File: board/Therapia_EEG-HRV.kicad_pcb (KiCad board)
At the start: 4 copper layers, 61.8 x 45 mm, 135 parts

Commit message: S4a: synthesize the 6 NPTH holes and close the board outline
13_fix_import.py repairs three EasyEDA-importer artefacts:
- the four M2 mounting holes were PTH pads; they become NPTH H1..H4,
  excluded from BOM/POS
- the two USB-C pegs were Edge.Cuts polygons owned by J1; they become
  standalone NPTH footprints PEG1/PEG2 at the same centres
- the board outline arrived as three open segments (EasyEDA holds it as one
  closed POLY); the rectangle is redrawn at the exact 2434x1772 mil size

Gate gates/S4a.json 10/10: NPTH 6 holes matching the 2026-08-16 DRL within
2um, PTH 16 and vias 238 unchanged, Edge.Cuts exactly 4 segments.
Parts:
- added PEG1: NPTH_0.7000mm_peg, NPTH_0.7mm_USB-C_peg, F.Cu at (176.9, 113.9)
- added PEG2: NPTH_0.7000mm_peg, NPTH_0.7mm_USB-C_peg, F.Cu at (176.9, 108.1)
- H1, H2, H3, H4: renamed from ?; value (none) -> NPTH_2.3876mm_M2

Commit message: S3: freeze ACCEPTANCE.md, generate the JLC rules, prove they see L1-L4
- ACCEPTANCE.md defines 'ready to order' as gates A..G; it is the spec the
  final check will implement. Records one deliberate deviation from the brief:
  pad_to_mask_clearance 0.0508 not 0.1016, because 4 mil per side leaves a
  0.0168 mm mask dam on the ADS1299's 0.5 mm pitch.
- 14_make_rules.py generates .kicad_pro + .kicad_dru + the board (setup) block
  from one table. Cross-checks contract/easyeda_rules.json and shows EasyEDA
  labels those values mm while storing mil (defInner 6.0039 -> 0.305 mm drill).
- 15_gate_s3.py runs DRC and requires L1..L4 to come back out of it. All four
  are reported, each at 0.0000 mm actual clearance.
- lib/drc.py: kicad-cli DRC is not deterministic (523/525/526 on identical
  input), so gates compare (type, nets, refs) signatures, not counts.

DRC baseline with JLC rules: 526 violations, 68 error, 0 unconnected
(was 1025/545 against KiCad defaults).
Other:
- rule pad_to_mask_clearance: 0 -> 0.0508
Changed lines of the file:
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@@
 	)
 	(setup
-		(pad_to_mask_clearance 0)
+		(pad_to_paste_clearance 0)
+		(solder_mask_min_width 0.0508)
+		(pad_to_mask_clearance 0.0508)
 		(allow_soldermask_bridges_in_footprints no)
 		(tenting

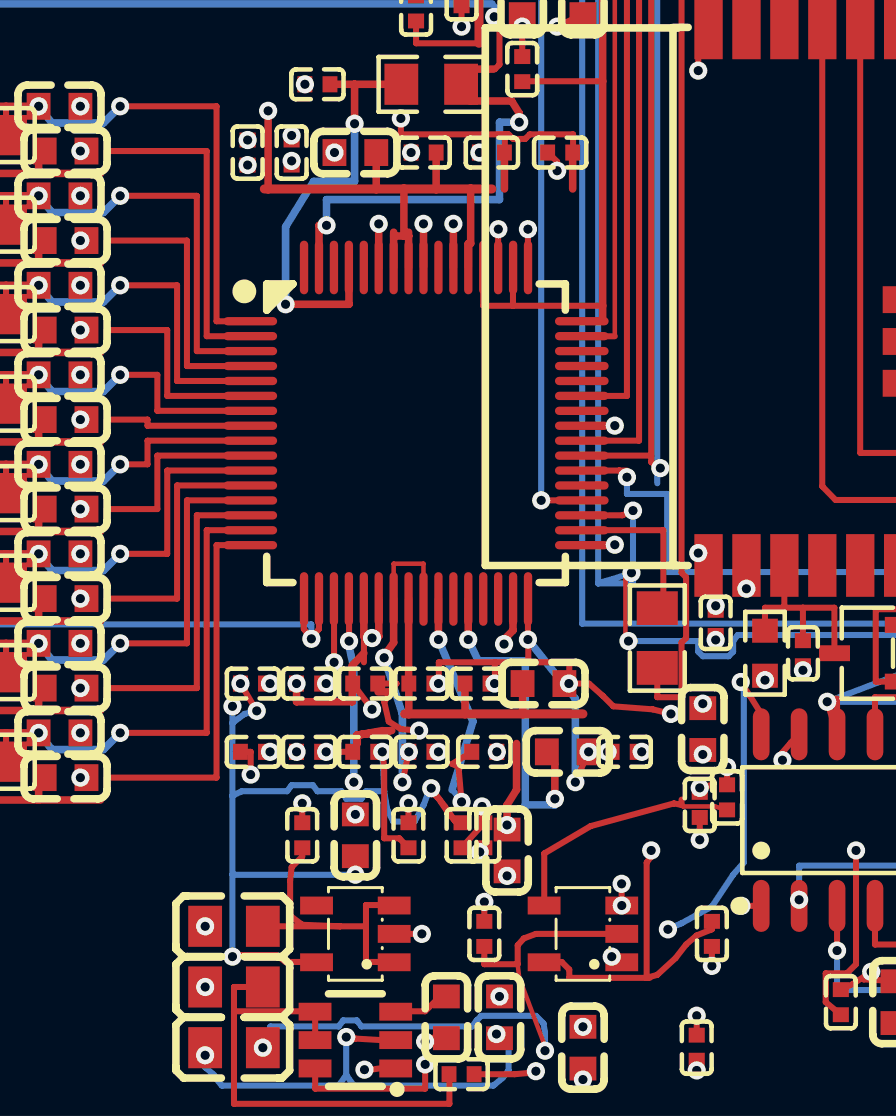
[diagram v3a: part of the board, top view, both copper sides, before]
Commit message: S4: apply ECO-1/2/3 to the PCB
ECO-1 (8 pins): TPS72325 EN moves off GND onto V_NLDO_IN -- the fatal B1 that
kept AVSS from ever coming up -- plus RESV1 to GND, GPIO1-4 bundled to the
adjacent GND pin, and VCAP2/VCAP3 onto new nets.
ECO-1 (4 parts): C_VCAP2/C_VCAP3/C_VCAP3_H/C_VCAP1_H placed and routed.
ECO-3 (2 parts): C_VCAP1 and C_VREFP_10u to 1206. Both only fit rotated 90.
ECO-2: values and LCSC numbers, no copper change. All 135 parts now carry
Value/MPN/LCSC from data/parts_lcsc.csv.

Result: pad net map == contract (0 diffs), 0 unconnected, DRC errors equal to
the pre-ECO baseline. Parts 137->141, tracks 1191->1213, vias 238->240.

lib/route.py does the geometry: every track, via and footprint position is
checked against the real copper at the design-rule clearance before it is
placed, and a step that cannot be satisfied is reported rather than forced.
lib/drc.py compares DRC reports by (type, nets) signature because kicad-cli
returns 525-531 violations for the same board on consecutive runs.
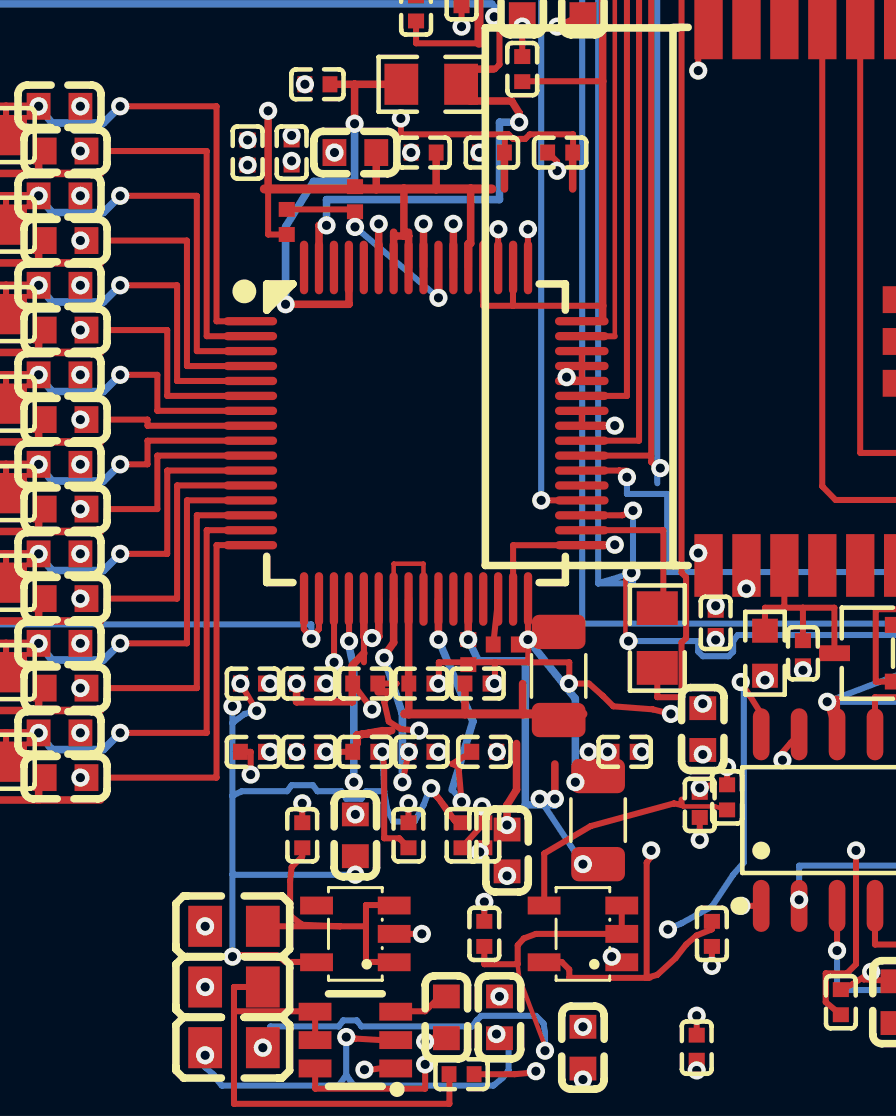
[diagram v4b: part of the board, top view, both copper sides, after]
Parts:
- removed the C_VREFP_10u at (150.4, 110.5)
- added C_VCAP1_H: 100nF, ProPrj_The-easyedapro:C0402, F.Cu at (147.9, 109.4)
- added C_VCAP2: 1uF, ProPrj_The-easyedapro:C0402, F.Cu at (149.2, 109.2)
- added C_VCAP3: 1uF, ProPrj_The-easyedapro:C0402, F.Cu at (144.1, 94.3)
- added C_VCAP3_H: 100nF, ProPrj_The-easyedapro:C0402, F.Cu at (141.8, 95.0)
- added C_VREFP_10u: 10uF_25V, C_1206_3216Metric, F.Cu at (150.9, 110.2)
- AMS1117: value (none) -> AMS1117-3.3
- C_3V3_B, C_3V3_B2, C_3V3_OUT, C_AVDD1_10u, C_AVDD_B, C_AVSS_B, C_BULK, C_DVDD_10u, C_DVDD_B, C_LM_FLY, C_LM_OUT, C_USB5V_B: value (none) -> 10uF
- C_3V3_H, C_3V3_H2, C_AVDD1_100n, C_AVDD_H, C_AVDD_P19, C_AVDD_P3, C_AVDD_P31, C_AVDD_P36, C_AVDD_P59, C_AVDD_P64, C_AVSS_H, C_AVSS_P17, C_AVSS_P30, C_AVSS_P37, C_AVSS_P60, C_BIAS_INV, C_DVDD_H, C_DVDD_P40, C_DVDD_P58, C_EN_DLY, C_HF, C_RST_DLY, C_USB5V_H, C_USB_V3, C_USB_VCC, C_VREFP_100n: value (none) -> 100nF
- C_3V3_IN, C_3V3_M, C_AVDD1_1u, C_LM_IN, C_NLDO_IN, C_PLDO_IN, C_PLDO_OUT, C_VCAP4: value (none) -> 1uF
- C_AVDD1_10n, C_VREFP_10n: value (none) -> 100pF
- C_CM1N, C_CM1P, C_CM2N, C_CM2P, C_CM3N, C_CM3P, C_CM4N, C_CM4P, C_CM5N, C_CM5P, C_CM6N, C_CM6P, C_CM7N, C_CM7P, C_CM8N, C_CM8P: value (none) -> 1nF
- C_DIF1, C_DIF2, C_DIF3, C_DIF4, C_DIF5, C_DIF6, C_DIF7, C_DIF8: value (none) -> 10nF_NP0_50V
- C_NLDO_OUT: value (none) -> 2.2uF
- C_NR: value (none) -> 10nF
- C_VCAP1: value (none) -> 100uF; footprint ProPrj_The-easyedapro:C0603 -> C_1206_3216Metric
- D_ESD: value (none) -> USBLC6-2SC6
- D_LED: value (none) -> LED_Y
- F1: value (none) -> PTC_500mA
- FB1, FB2, FB3, FB4, FB5: value (none) -> FB_600R
- J1: value (none) -> USB-C_16P
- J2: value (none) -> Header_2x6
- LM2664: value (none) -> LM2664
- Q_EN, Q_IO0: value (none) -> S8050
- R_BIAS_FB, R_BIAS_SER: value (none) -> 1M
- R_CC1, R_CC2: value (none) -> 5.1k
- R_CS_UP, R_DRDY_UP, R_EN_UP, R_IN1N, R_IN1P, R_IN2N, R_IN2P, R_IN3N, R_IN3P, R_IN4N, R_IN4P, R_IN5N, R_IN5P, R_IN6N, R_IN6P, R_IN7N, R_IN7P, R_IN8N, R_IN8P, R_IO0_UP, R_IO15_DN, R_IO2_DN, R_PWDN_UP, R_Q_EN_B, R_Q_IO0_B, R_RST_UP, R_START_DN: value (none) -> 10k
- R_LED: value (none) -> 330R
- R_MISO, R_MOSI, R_SCLK, R_SRB_SER: value (none) -> 0R
- TLV70025: value (none) -> TLV70025
- TPS72325: value (none) -> TPS72325
- U_ADS: value (none) -> ADS1299
- U_MCU: value (none) -> ESP32-WROOM-32E-N4
- U_USB: value (none) -> CH340C
- moved C_VCAP1 2.50 mm to (152.3, 115.1), turned to 90 degrees
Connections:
- TPS72325 pad 3: GND -> V_NLDO_IN
- U_ADS pad 30: (no net) -> VCAP2
- U_ADS pad 31: AVDD -> GND
- U_ADS pad 42: (no net) -> GND
- U_ADS pad 44: (no net) -> GND
- U_ADS pad 45: (no net) -> GND
- U_ADS pad 46: (no net) -> GND
- U_ADS pad 55: (no net) -> VCAP3
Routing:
- net VCAP3: track 0.00 -> 7.55 mm, vias 0 -> 2
- net GND: track 80.4 -> 85.8 mm, vias 82 -> 81
- net AVSS: track 82.4 -> 87.3 mm
- net VCAP1: track 10.9 -> 14.5 mm, vias 2 -> 4
- net VCAP2: track 0.00 -> 1.53 mm
- net AVDD: track 53.5 -> 52.0 mm, vias 21 -> 20
- net V_NLDO_IN: track 20.0 -> 21.0 mm
